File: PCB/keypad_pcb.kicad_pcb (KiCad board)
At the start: 2 copper layers, 100 x 80 mm, 35 parts, among them J1 Conn_01x04, SW1 SW_Push, SW2 SW_Push, SW3 SW_Push, SW4 SW_Push, SW5 SW_Push, SW6 SW_Push, SW8 RotaryEncoder_Switch, U1 XIAO-RP2040-DIP

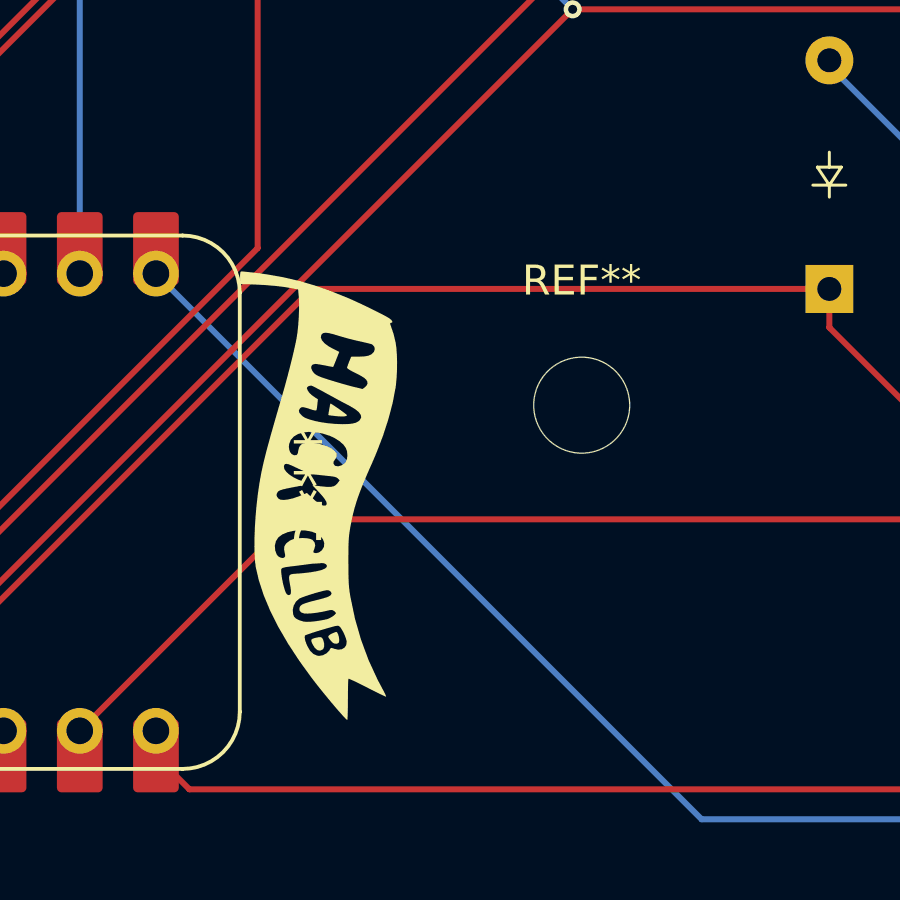
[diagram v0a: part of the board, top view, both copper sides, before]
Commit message: case update
i have updated case and fixed the shape
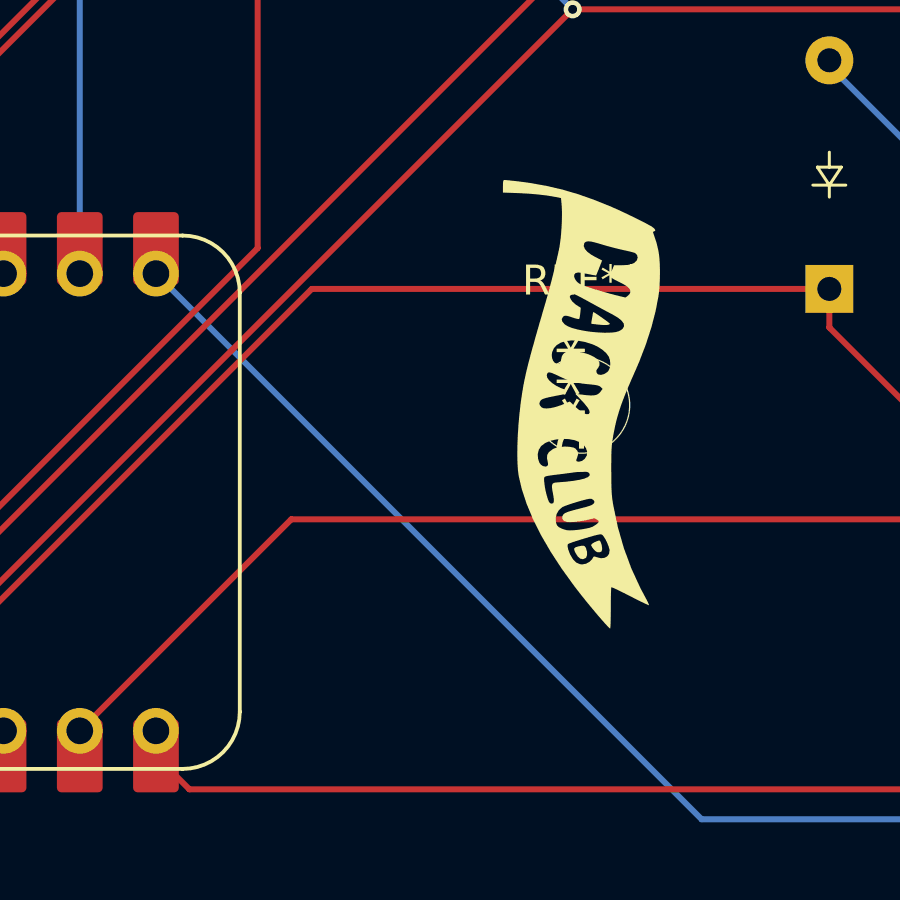
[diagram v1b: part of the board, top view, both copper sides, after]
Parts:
- moved G*** 9.28 mm to (48.8, 76.9)
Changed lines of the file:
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@@
 	(footprint "pcb art:hackclub_17mm"
 		(layer "F.Cu")
-		(at 40.06925 79.9605 -90)
+		(at 48.83225 76.9125 -90)
 		(property "Reference" "G***"
 			(at 0 0 90)
